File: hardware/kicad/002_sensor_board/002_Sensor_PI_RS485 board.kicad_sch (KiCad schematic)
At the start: 78 parts, among them J1 JST_SH, J2 JST_SH, J3 USB_C_Receptacle_USB2.0, U1 RP2354_60QFN, U4 TPD4E05U06DQAR, U5 THVD1424RGTR, U6 TPS62A0569ADRLR, Y1 ABM8-272-T3

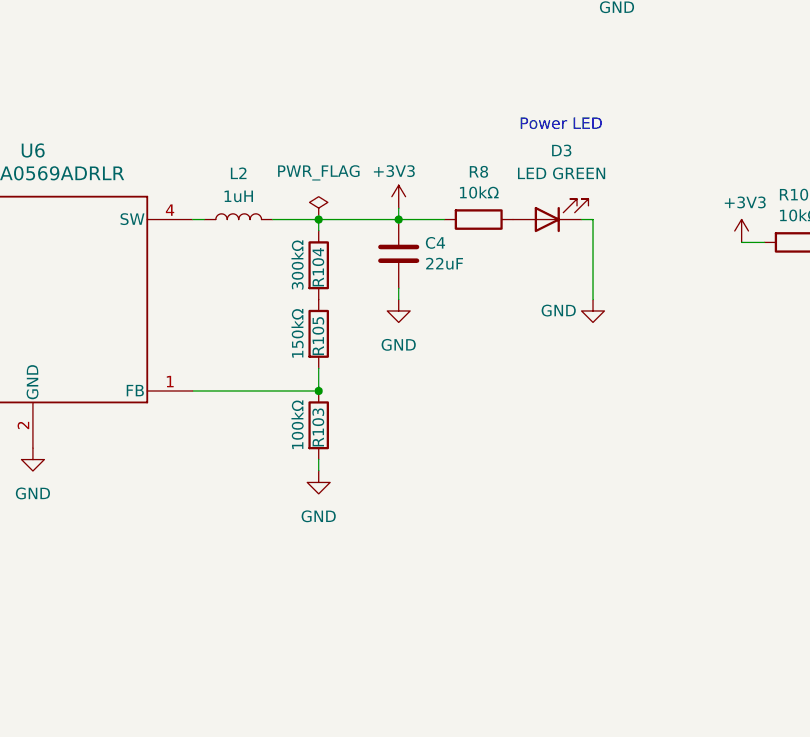
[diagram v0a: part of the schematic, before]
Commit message: 002 sensor board: Rev B ordered; rename folder, add schematic PDF
Board is at zero ERC and zero DRC and has shipped to fab as Rev B
(RS-485, 5 V bus). This commit captures exactly what was ordered.

- Rename 002_sensor_board_example -> 002_sensor_board. It stopped being
  an example some time ago.
- Add Schematic_revB.pdf.
- Replace the Rev A production outputs with the Rev B set actually sent:
  gerbers/drill zip, BOM, positions, designators, IPC netlist.

The BOM now carries LCSC part numbers for every specialty part, which
none of the previous exports did - VCNT2025X01 (C7431257) and
THVD1424RGTR (C5359161) in particular had only ever been matched in
JLC's web UI at order time, so they survived in neither the design, the
exports, nor 34 KiCad backups. Recorded in the schematic this time.

Values were normalised earlier today (no space before units, ASCII u,
3.3u given its missing unit), which merged 100 kohm/100kohm and
1 uF/1uF into single BOM lines.

Excluded: production_rev B.zip, a Finder-created archive of the
production folder carrying __MACOSX resource forks and a .DS_Store. The
real fab deliverable is production/*.zip.

Co-Authored-By: Claude Opus 5 <noreply@anthropic.com>
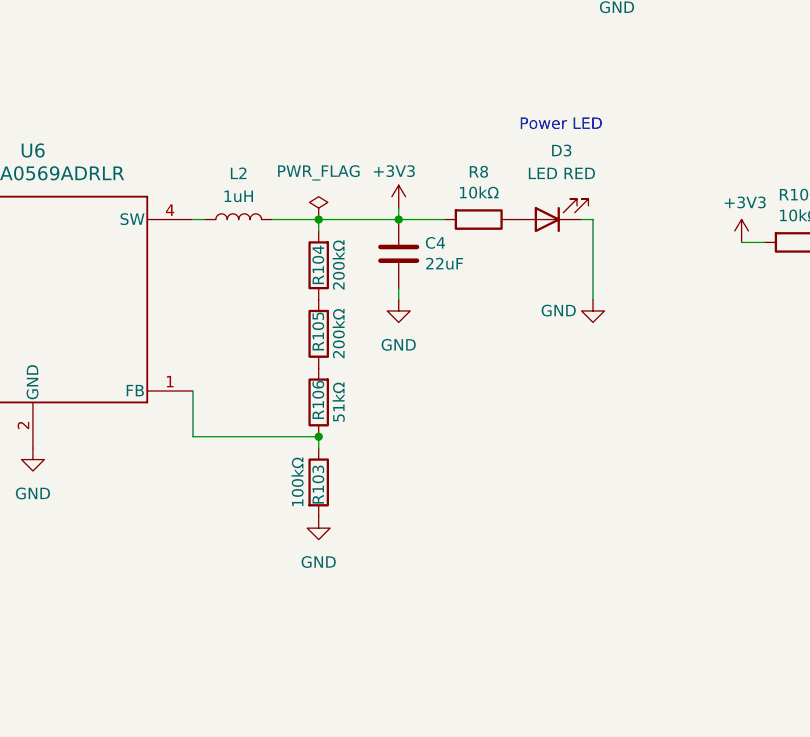
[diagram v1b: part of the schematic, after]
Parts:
- added R106: 51kΩ, Resistor_SMD:R_0402_1005Metric, symbol Device:R
- D3: value LED GREEN -> LED RED; footprint LED_SMD:LED_0402_1005Metric -> LED_SMD:LED_0603_1608Metric; JLCPCB Part # C130722 -> C2286
- R104: value 300kΩ -> 200kΩ
- R105: value 150kΩ -> 200kΩ
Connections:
- net +3V3: now also R104.2; no longer R104.1
- net at R105.1: now also R106.2; no longer R104.2
- net at R103.1, U6.1 (FB): now also R106.1; no longer R105.2
- new net: R104.1, R105.2
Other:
- moved on the sheet: R103, R104, R105

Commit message: Consolidate footprints into a single shared library
All three boards carried their own copies of the same footprints - 79
files across 11 project libraries for 37 distinct footprints. Several
existed three times over (RP2350-QFN-60 ThermalVias, edge_holes,
TO-236_VIS-L, SON_NT2020_VIS, L_pol_2016, USB_Micro-B). Three copies
drift, and this project has already been bitten twice by a library and
a board disagreeing.

- New hardware/kicad/common.pretty holds all 37, verified byte-identical
  where they were duplicated: zero name collisions with differing
  content, so nothing had to be reconciled.
- Each board's fp-lib-table is now a single "common" entry. Previously
  001 alone had eight, and the nickname "footprints" meant a different
  library on each of the three boards - so lib_ids were rewritten per
  board, not globally.
- 459 footprint references across the three boards now resolve. That
  includes SparkFun-Qwiic:qwiic_8mm on 001, which was referenced but
  had never been in any fp-lib-table - broken before this change.

Also shrinks docs/images/reflective_sensor.png from 2816x1536 / 4.43 MB
to 1600x873 / 1.72 MB.

Co-Authored-By: Claude Opus 5 <noreply@anthropic.com>
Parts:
- C2, C3: footprint footprints:C_0402_1005Metric_small_pads -> common:C_0402_1005Metric_small_pads
- CR1: footprint footprints:SOD-323_L1.8-W1.3-LS2.5-RD -> common:SOD-323_L1.8-W1.3-LS2.5-RD
- H1, H10, H11, H12, H13, H14, H15, H16, H17, H18, H2, H3, H4, H5, H6, H7, H8, H9: footprint footprints:MountingHole_2.7mm_M2.5_Keepout -> common:MountingHole_2.7mm_M2.5_Keepout
- L1: footprint footprints:L_pol_2016 -> common:L_pol_2016
- U1: footprint footprints:RP2350-QFN-60-1EP_7x7_P0.4mm_EP3.4x3.4mm_ThermalVias -> common:RP2350-QFN-60-1EP_7x7_P0.4mm_EP3.4x3.4mm_ThermalVias
- U4: footprint footprints:DQA0010A -> common:DQA0010A
- U5: footprint footprints:QFN_24RGTR_TEX -> common:QFN_24RGTR_TEX
- U6: footprint footprints:SOT-563_DRL0006A -> common:SOT-563_DRL0006A
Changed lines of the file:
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@@
 			)
 		)
-		(property "Footprint" "footprints:MountingHole_2.7mm_M2.5_Keepout"
+		(property "Footprint" "common:MountingHole_2.7mm_M2.5_Keepout"
 			(at 105.41 44.45 0)
 			(hide yes)
@@
 			)
 		)
-		(property "Footprint" "footprints:MountingHole_2.7mm_M2.5_Keepout"
+		(property "Footprint" "common:MountingHole_2.7mm_M2.5_Keepout"
 			(at 128.27 19.05 0)
 			(hide yes)
@@
 			)
 		)
-		(property "Footprint" "footprints:MountingHole_2.7mm_M2.5_Keepout"
+		(property "Footprint" "common:MountingHole_2.7mm_M2.5_Keepout"
 			(at 105.41 27.94 0)
 			(hide yes)
@@
 			)
 		)
-		(property "Footprint" "footprints:MountingHole_2.7mm_M2.5_Keepout"
+		(property "Footprint" "common:MountingHole_2.7mm_M2.5_Keepout"
 			(at 128.27 60.96 0)
 			(hide yes)
@@
 			)
 		)
-		(property "Footprint" "footprints:MountingHole_2.7mm_M2.5_Keepout"
+		(property "Footprint" "common:MountingHole_2.7mm_M2.5_Keepout"
 			(at 105.41 60.96 0)
 			(hide yes)
@@
 			)
 		)
-		(property "Footprint" "footprints:SOD-323_L1.8-W1.3-LS2.5-RD"
+		(property "Footprint" "common:SOD-323_L1.8-W1.3-LS2.5-RD"
 			(at 58.42 106.68 0)
 			(hide yes)
@@
 			)
 		)
-		(property "Footprint" "footprints:MountingHole_2.7mm_M2.5_Keepout"
+		(property "Footprint" "common:MountingHole_2.7mm_M2.5_Keepout"
 			(at 128.27 36.83 0)
 			(hide yes)
@@
 			)
 		)
-		(property "Footprint" "footprints:MountingHole_2.7mm_M2.5_Keepout"
+		(property "Footprint" "common:MountingHole_2.7mm_M2.5_Keepout"
 			(at 153.67 27.94 0)
 			(hide yes)
@@
 			)
 		)
-		(property "Footprint" "footprints:MountingHole_2.7mm_M2.5_Keepout"
+		(property "Footprint" "common:MountingHole_2.7mm_M2.5_Keepout"
 			(at 128.27 27.94 0)
 			(hide yes)
@@
 			)
 		)
-		(property "Footprint" "footprints:SOT-563_DRL0006A"
+		(property "Footprint" "common:SOT-563_DRL0006A"
 			(at 130.81 124.46 0)
 			(hide yes)
@@
 			)
 		)
-		(property "Footprint" "footprints:MountingHole_2.7mm_M2.5_Keepout"
+		(property "Footprint" "common:MountingHole_2.7mm_M2.5_Keepout"
 			(at 128.27 52.07 0)
 			(hide yes)
@@
 			)
 		)
-		(property "Footprint" "footprints:C_0402_1005Metric_small_pads"
+		(property "Footprint" "common:C_0402_1005Metric_small_pads"
 			(at 194.0052 71.12 0)
 			(hide yes)
@@
 			)
 		)
-		(property "Footprint" "footprints:MountingHole_2.7mm_M2.5_Keepout"
+		(property "Footprint" "common:MountingHole_2.7mm_M2.5_Keepout"
 			(at 128.27 77.47 0)
 			(hide yes)
@@
 			)
 		)
-		(property "Footprint" "footprints:MountingHole_2.7mm_M2.5_Keepout"
+		(property "Footprint" "common:MountingHole_2.7mm_M2.5_Keepout"
 			(at 153.67 19.05 0)
 			(hide yes)
@@
 			)
 		)
-		(property "Footprint" "footprints:MountingHole_2.7mm_M2.5_Keepout"
+		(property "Footprint" "common:MountingHole_2.7mm_M2.5_Keepout"
 			(at 128.27 44.45 0)
 			(hide yes)
@@
 			)
 		)
-		(property "Footprint" "footprints:RP2350-QFN-60-1EP_7x7_P0.4mm_EP3.4x3.4mm_ThermalVias"
+		(property "Footprint" "common:RP2350-QFN-60-1EP_7x7_P0.4mm_EP3.4x3.4mm_ThermalVias"
 			(at 264.16 104.14 0)
 			(hide yes)
@@
 			)
 		)
-		(property "Footprint" "footprints:MountingHole_2.7mm_M2.5_Keepout"
+		(property "Footprint" "common:MountingHole_2.7mm_M2.5_Keepout"
 			(at 105.41 77.47 0)
 			(hide yes)
@@
 			)
 		)
-		(property "Footprint" "footprints:MountingHole_2.7mm_M2.5_Keepout"
+		(property "Footprint" "common:MountingHole_2.7mm_M2.5_Keepout"
 			(at 105.41 36.83 0)
 			(hide yes)
@@
 			)
 		)
-		(property "Footprint" "footprints:MountingHole_2.7mm_M2.5_Keepout"
+		(property "Footprint" "common:MountingHole_2.7mm_M2.5_Keepout"
 			(at 105.41 69.85 0)
 			(hide yes)
@@
 			)
 		)
-		(property "Footprint" "footprints:MountingHole_2.7mm_M2.5_Keepout"
+		(property "Footprint" "common:MountingHole_2.7mm_M2.5_Keepout"
 			(at 105.41 19.05 0)
 			(hide yes)
@@
 			)
 		)
-		(property "Footprint" "footprints:L_pol_2016"
+		(property "Footprint" "common:L_pol_2016"
 			(at 219.71 67.31 0)
 			(hide yes)
@@
 			)
 		)
-		(property "Footprint" "footprints:MountingHole_2.7mm_M2.5_Keepout"
+		(property "Footprint" "common:MountingHole_2.7mm_M2.5_Keepout"
 			(at 128.27 69.85 0)
 			(hide yes)
@@
 			)
 		)
-		(property "Footprint" "footprints:MountingHole_2.7mm_M2.5_Keepout"
+		(property "Footprint" "common:MountingHole_2.7mm_M2.5_Keepout"
 			(at 105.41 52.07 0)
 			(hide yes)
@@
 			)
 		)
-		(property "Footprint" "footprints:DQA0010A"
+		(property "Footprint" "common:DQA0010A"
 			(at 71.12 167.64 0)
 			(hide yes)
@@
 			)
 		)
-		(property "Footprint" "footprints:QFN_24RGTR_TEX"
+		(property "Footprint" "common:QFN_24RGTR_TEX"
 			(at 167.64 233.68 0)
 			(hide yes)
@@
 			)
 		)
-		(property "Footprint" "footprints:C_0402_1005Metric_small_pads"
+		(property "Footprint" "common:C_0402_1005Metric_small_pads"
 			(at 205.4352 71.12 0)
 			(hide yes)

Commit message: Rename shared footprint library common -> photon_common
'common' is too generic for a library nickname - it can collide with a
global library or another project's table, and it doesn't identify whose
footprints these are.

155 lib_ids rewritten across the three boards plus all three
fp-lib-tables. All 459 footprint references still resolve.

Co-Authored-By: Claude Opus 5 <noreply@anthropic.com>
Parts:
- C2, C3: footprint common:C_0402_1005Metric_small_pads -> photon_common:C_0402_1005Metric_small_pads
- CR1: footprint common:SOD-323_L1.8-W1.3-LS2.5-RD -> photon_common:SOD-323_L1.8-W1.3-LS2.5-RD
- H1, H10, H11, H12, H13, H14, H15, H16, H17, H18, H2, H3, H4, H5, H6, H7, H8, H9: footprint common:MountingHole_2.7mm_M2.5_Keepout -> photon_common:MountingHole_2.7mm_M2.5_Keepout
- L1: footprint common:L_pol_2016 -> photon_common:L_pol_2016
- U1: footprint common:RP2350-QFN-60-1EP_7x7_P0.4mm_EP3.4x3.4mm_ThermalVias -> photon_common:RP2350-QFN-60-1EP_7x7_P0.4mm_EP3.4x3.4mm_ThermalVias
- U4: footprint common:DQA0010A -> photon_common:DQA0010A
- U5: footprint common:QFN_24RGTR_TEX -> photon_common:QFN_24RGTR_TEX
- U6: footprint common:SOT-563_DRL0006A -> photon_common:SOT-563_DRL0006A
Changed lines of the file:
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@@
 			)
 		)
-		(property "Footprint" "common:MountingHole_2.7mm_M2.5_Keepout"
+		(property "Footprint" "photon_common:MountingHole_2.7mm_M2.5_Keepout"
 			(at 105.41 44.45 0)
 			(hide yes)
@@
 			)
 		)
-		(property "Footprint" "common:MountingHole_2.7mm_M2.5_Keepout"
+		(property "Footprint" "photon_common:MountingHole_2.7mm_M2.5_Keepout"
 			(at 128.27 19.05 0)
 			(hide yes)
@@
 			)
 		)
-		(property "Footprint" "common:MountingHole_2.7mm_M2.5_Keepout"
+		(property "Footprint" "photon_common:MountingHole_2.7mm_M2.5_Keepout"
 			(at 105.41 27.94 0)
 			(hide yes)
@@
 			)
 		)
-		(property "Footprint" "common:MountingHole_2.7mm_M2.5_Keepout"
+		(property "Footprint" "photon_common:MountingHole_2.7mm_M2.5_Keepout"
 			(at 128.27 60.96 0)
 			(hide yes)
@@
 			)
 		)
-		(property "Footprint" "common:MountingHole_2.7mm_M2.5_Keepout"
+		(property "Footprint" "photon_common:MountingHole_2.7mm_M2.5_Keepout"
 			(at 105.41 60.96 0)
 			(hide yes)
@@
 			)
 		)
-		(property "Footprint" "common:SOD-323_L1.8-W1.3-LS2.5-RD"
+		(property "Footprint" "photon_common:SOD-323_L1.8-W1.3-LS2.5-RD"
 			(at 58.42 106.68 0)
 			(hide yes)
@@
 			)
 		)
-		(property "Footprint" "common:MountingHole_2.7mm_M2.5_Keepout"
+		(property "Footprint" "photon_common:MountingHole_2.7mm_M2.5_Keepout"
 			(at 128.27 36.83 0)
 			(hide yes)
@@
 			)
 		)
-		(property "Footprint" "common:MountingHole_2.7mm_M2.5_Keepout"
+		(property "Footprint" "photon_common:MountingHole_2.7mm_M2.5_Keepout"
 			(at 153.67 27.94 0)
 			(hide yes)
@@
 			)
 		)
-		(property "Footprint" "common:MountingHole_2.7mm_M2.5_Keepout"
+		(property "Footprint" "photon_common:MountingHole_2.7mm_M2.5_Keepout"
 			(at 128.27 27.94 0)
 			(hide yes)
@@
 			)
 		)
-		(property "Footprint" "common:SOT-563_DRL0006A"
+		(property "Footprint" "photon_common:SOT-563_DRL0006A"
 			(at 130.81 124.46 0)
 			(hide yes)
@@
 			)
 		)
-		(property "Footprint" "common:MountingHole_2.7mm_M2.5_Keepout"
+		(property "Footprint" "photon_common:MountingHole_2.7mm_M2.5_Keepout"
 			(at 128.27 52.07 0)
 			(hide yes)
@@
 			)
 		)
-		(property "Footprint" "common:C_0402_1005Metric_small_pads"
+		(property "Footprint" "photon_common:C_0402_1005Metric_small_pads"
 			(at 194.0052 71.12 0)
 			(hide yes)
@@
 			)
 		)
-		(property "Footprint" "common:MountingHole_2.7mm_M2.5_Keepout"
+		(property "Footprint" "photon_common:MountingHole_2.7mm_M2.5_Keepout"
 			(at 128.27 77.47 0)
 			(hide yes)
@@
 			)
 		)
-		(property "Footprint" "common:MountingHole_2.7mm_M2.5_Keepout"
+		(property "Footprint" "photon_common:MountingHole_2.7mm_M2.5_Keepout"
 			(at 153.67 19.05 0)
 			(hide yes)
@@
 			)
 		)
-		(property "Footprint" "common:MountingHole_2.7mm_M2.5_Keepout"
+		(property "Footprint" "photon_common:MountingHole_2.7mm_M2.5_Keepout"
 			(at 128.27 44.45 0)
 			(hide yes)
@@
 			)
 		)
-		(property "Footprint" "common:RP2350-QFN-60-1EP_7x7_P0.4mm_EP3.4x3.4mm_ThermalVias"
+		(property "Footprint" "photon_common:RP2350-QFN-60-1EP_7x7_P0.4mm_EP3.4x3.4mm_ThermalVias"
 			(at 264.16 104.14 0)
 			(hide yes)
@@
 			)
 		)
-		(property "Footprint" "common:MountingHole_2.7mm_M2.5_Keepout"
+		(property "Footprint" "photon_common:MountingHole_2.7mm_M2.5_Keepout"
 			(at 105.41 77.47 0)
 			(hide yes)
@@
 			)
 		)
-		(property "Footprint" "common:MountingHole_2.7mm_M2.5_Keepout"
+		(property "Footprint" "photon_common:MountingHole_2.7mm_M2.5_Keepout"
 			(at 105.41 36.83 0)
 			(hide yes)
@@
 			)
 		)
-		(property "Footprint" "common:MountingHole_2.7mm_M2.5_Keepout"
+		(property "Footprint" "photon_common:MountingHole_2.7mm_M2.5_Keepout"
 			(at 105.41 69.85 0)
 			(hide yes)
@@
 			)
 		)
-		(property "Footprint" "common:MountingHole_2.7mm_M2.5_Keepout"
+		(property "Footprint" "photon_common:MountingHole_2.7mm_M2.5_Keepout"
 			(at 105.41 19.05 0)
 			(hide yes)
@@
 			)
 		)
-		(property "Footprint" "common:L_pol_2016"
+		(property "Footprint" "photon_common:L_pol_2016"
 			(at 219.71 67.31 0)
 			(hide yes)
@@
 			)
 		)
-		(property "Footprint" "common:MountingHole_2.7mm_M2.5_Keepout"
+		(property "Footprint" "photon_common:MountingHole_2.7mm_M2.5_Keepout"
 			(at 128.27 69.85 0)
 			(hide yes)
@@
 			)
 		)
-		(property "Footprint" "common:MountingHole_2.7mm_M2.5_Keepout"
+		(property "Footprint" "photon_common:MountingHole_2.7mm_M2.5_Keepout"
 			(at 105.41 52.07 0)
 			(hide yes)
@@
 			)
 		)
-		(property "Footprint" "common:DQA0010A"
+		(property "Footprint" "photon_common:DQA0010A"
 			(at 71.12 167.64 0)
 			(hide yes)
@@
 			)
 		)
-		(property "Footprint" "common:QFN_24RGTR_TEX"
+		(property "Footprint" "photon_common:QFN_24RGTR_TEX"
 			(at 167.64 233.68 0)
 			(hide yes)
@@
 			)
 		)
-		(property "Footprint" "common:C_0402_1005Metric_small_pads"
+		(property "Footprint" "photon_common:C_0402_1005Metric_small_pads"
 			(at 205.4352 71.12 0)
 			(hide yes)
